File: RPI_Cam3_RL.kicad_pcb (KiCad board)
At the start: 2 copper layers, 106 x 106 mm, 42 parts, among them J1 in, Q1 2N7002, U1 RPI_CAM_3

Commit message: Updated Pcb Design -Small Radius
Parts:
- C1, C2, DP1, F1, J1, JP1, Q1, RP1, RP2: moved to B.Cu
- moved C1 116.1 mm to (218.9, 111.1)
- moved C2 115.7 mm to (216.2, 111.1)
- moved H8 115.1 mm to (225.5, 111.5)
- moved Q1 113.7 mm to (218.9, 120.7)
- moved JP1 111.8 mm to (213.5, 111.2), turned to 90 degrees
- moved RP2 111.7 mm to (215.2, 116.4)
- moved H6 111.6 mm to (225.5, 70.5)
- moved F1 109.8 mm to (210.7, 111.2), turned to -90 degrees
- moved RP1 106.5 mm to (212.5, 116.4)
- moved DP1 102.7 mm to (205.3, 111.2), turned to 180 degrees
- moved J1 91.6 mm to (202.6, 116.4), turned to 0 degrees
- moved H2 81.2 mm to (215.2, 88.8)
- moved R1 80.3 mm to (204.8, 57.0), turned to 0 degrees
- moved R12 80.2 mm to (187.8, 61.6), turned to 30 degrees
- moved R2 76.3 mm to (221.8, 61.6), turned to -30 degrees
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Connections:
- J1 pad 1: GND -> +5V
- J1 pad 3: +5V -> GND
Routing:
- net /EN: track 22.1 -> 12.4 mm
- net Net-(Q1-G): track 6.56 -> 13.2 mm
- net Net-(JP1-A): track 22.2 -> 15.6 mm
- net Net-(DP1-K): track 11.7 -> 6.91 mm
- net Net-(D4-A): track 5.91 -> 3.76 mm
- net Net-(D3-A): track 5.56 -> 3.76 mm
- net Net-(D7-A): track 6.02 -> 4.27 mm
- net Net-(D12-A): track 5.83 -> 4.17 mm
- net Net-(D8-A): track 6.16 -> 4.73 mm
- net Net-(D6-A): track 5.67 -> 4.27 mm
- net Net-(D9-A): track 5.94 -> 4.68 mm
- net Net-(D5-A): track 5.31 -> 4.08 mm
- net +5V: track 6.55 -> 5.49 mm
- net Net-(D11-A): track 5.69 -> 4.66 mm
- net Net-(D1-A): track 5.18 -> 4.17 mm
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- added copper zone on B.Cu, net Net-(Q1-S)
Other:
- board size 106 x 106 mm -> 76 x 76 mm

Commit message: design updates
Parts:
- added H10: m2, MountingHole:MountingHole_3.2mm_M3, F.Cu at (184.5, 91.4)
- added H9: m2, MountingHole:MountingHole_3.2mm_M3, F.Cu at (224.5, 91.4)
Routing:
- net /EN: track 12.4 -> 24.9 mm, vias 0 -> 1
- net Net-(Q1-S): vias 16 -> 24
- net GND: vias 25 -> 26

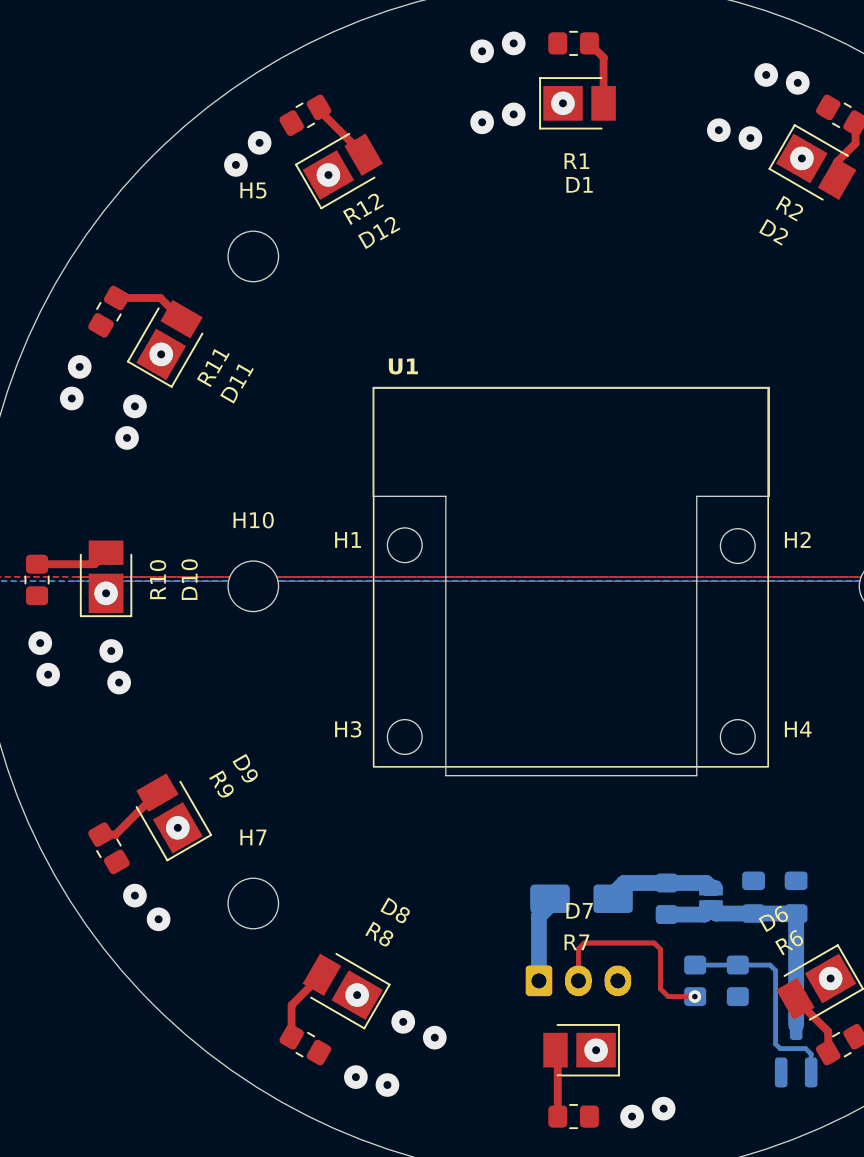
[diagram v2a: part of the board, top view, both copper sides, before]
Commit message: silkscreen updates
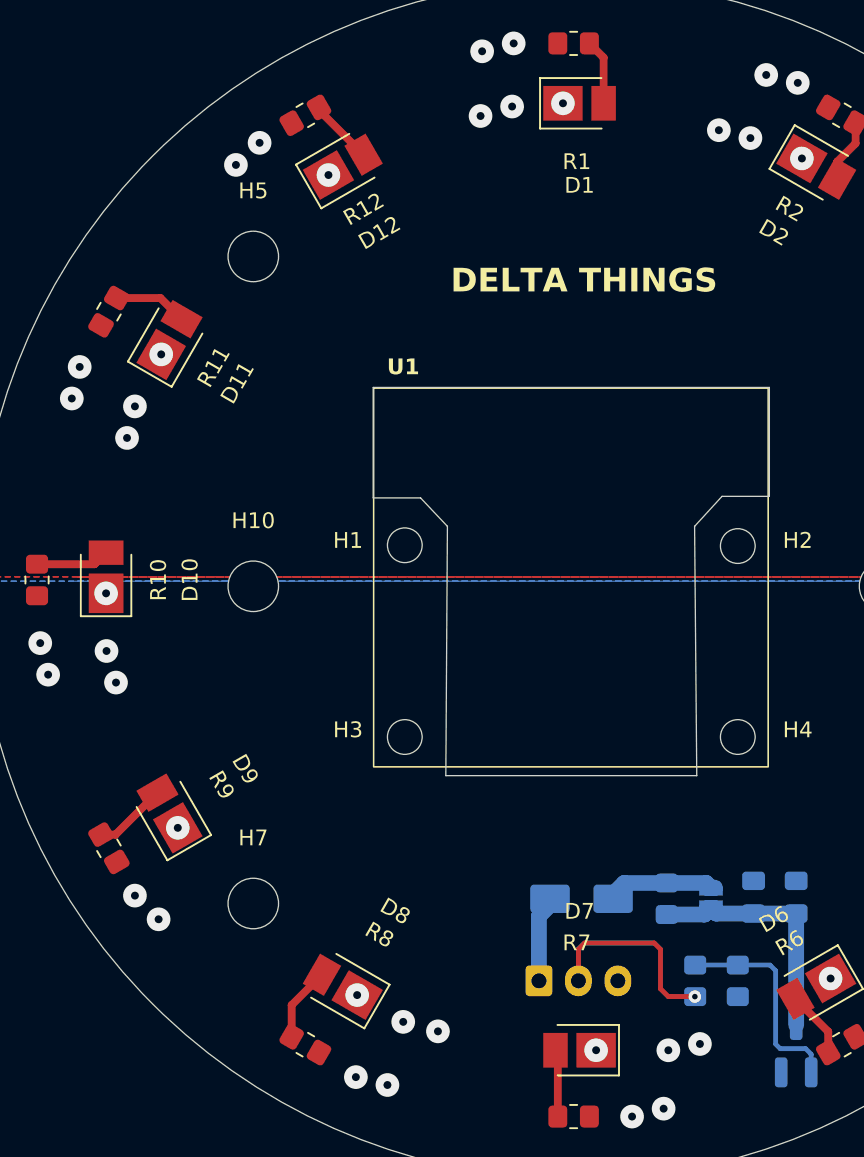
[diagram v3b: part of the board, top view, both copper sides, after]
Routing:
- net GND: vias 26 -> 28
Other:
- outline, holes or cut-outs redrawn
- board text added: "DELTA THINGS"
- board text added: "RPI_CAM_RingLight Rev 1.0.0 2026-01-07 Made In India"
